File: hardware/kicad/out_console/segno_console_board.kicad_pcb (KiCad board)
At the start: 2 copper layers, 130 x 90 mm, 53 parts, among them J1 RaspberryPi_Pico_Common_THT, J10 JST_XH_B2B-XH-A_1x02_P2.50mm_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, J11 JST_XH_B2B-XH-A_1x02_P2.50mm_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, J12 JST_XH_B2B-XH-A_1x02_P2.50mm_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, J13 JST_XH_B2B-XH-A_1x02_P2.50mm_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, J14 JST_XH_B2B-XH-A_1x02_P2.50mm_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, J15 JST_XH_B2B-XH-A_1x02_P2.50mm_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, J16 JST_XH_B2B-XH-A_1x02_P2.50mm_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, J17 JST_XH_B2B-XH-A_1x02_P2.50mm_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, J18 JST_XH_B2B-XH-A_1x02_P2.50mm_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, J19 JST_XH_B2B-XH-A_1x02_P2.50mm_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, J2 IDC-Header_2x20_P2.54mm_Verti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, J20 JST_XH_B3B-XH-A_1x03_P2.50mm_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, J21 JST_XH_B3B-XH-A_1x03_P2.50mm_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, J3 JST_XH_B4B-XH-A_1x04_P2.50mm_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, J4 JST_XH_B3B-XH-A_1x03_P2.50mm_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, J5 JST_XH_B2B-XH-A_1x02_P2.50mm_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, J6 JST_XH_B8B-XH-A_1x08_P2.50mm_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, J7 JST_XH_B3B-XH-A_1x03_P2.50mm_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, J8 JST_XH_B2B-XH-A_1x02_P2.50mm_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, J9 JST_XH_B3B-XH-A_1x03_P2.50mm_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, U1 DIP-14_W7.62mm, U2 DIP-6_W7.62mm

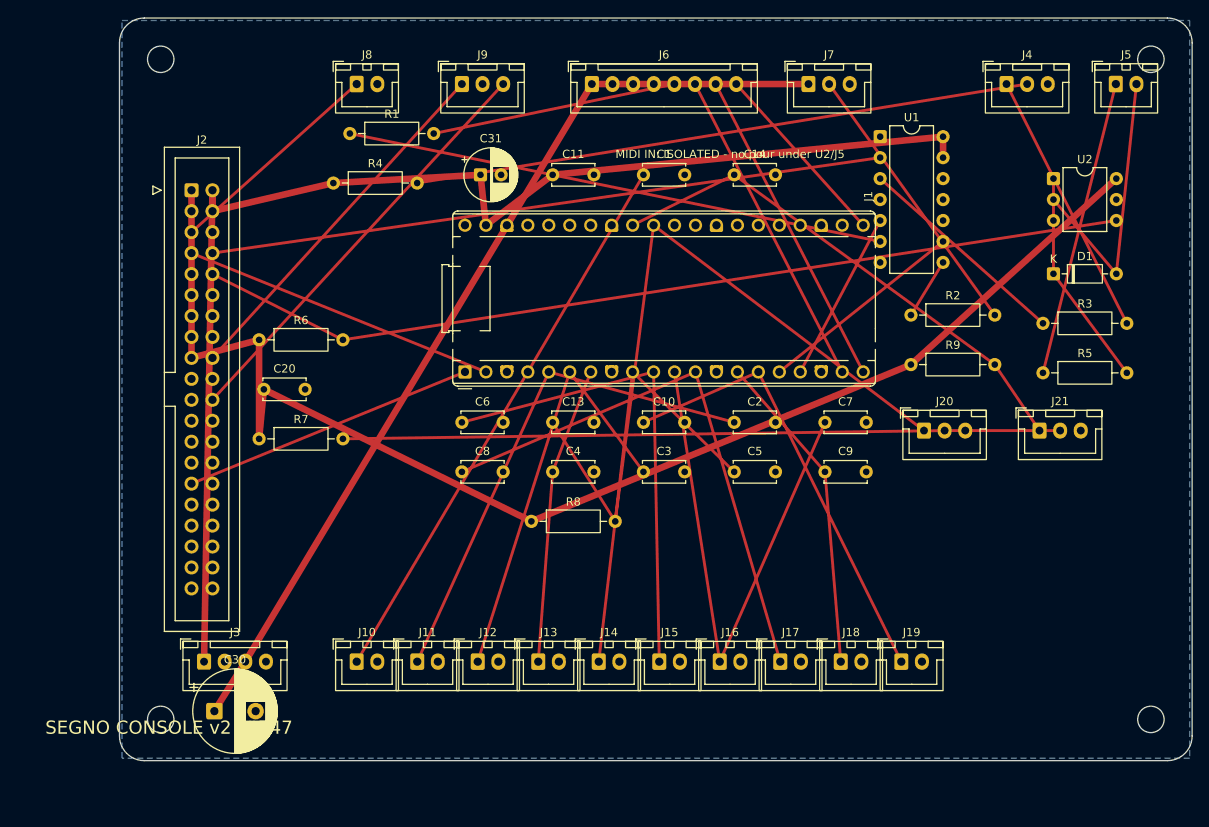
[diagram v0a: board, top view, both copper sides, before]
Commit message: feat(hardware): lay out the console board around its harness, not its schematic
The v2 board placed connectors wherever they fit. Reworked so the two things
that actually constrain it drive the layout:

- The pin map is half the floorplan. The module's pads 1..20 are one physical
  row and 21..40 the other, so a GPIO number decides where a connector can sit.
  LINK moves to GP16/17 (still a UART0 pair, now the end nearest the ribbon),
  the ring/encoder group onto four contiguous row-A pads, and gates enforce
  both. ENC_B used to run 42 mm diagonally across the board.
- Connectors group by where their CABLE goes. POWER, MIDI IN, MIDI OUT, CTRL 1
  and CTRL 2 all land on the rear panel, so they sit on one edge in the panel's
  own order, gated against rear_io_stations.json. The loom used to leave the
  board from two places.

Also: the Pi ribbon moves to the board edge (a 40-way leaving mid-board folds
back over everything), ground pours on both layers, every connector carries a
function label like segno_pedal_main does, and an expansion header exposes the
six GPIO that were being ERC-exempted into nothing.

115x95 mm, down from 160x100. 0 DRC violations, 0 unconnected.

New gates, each negative-controlled: RATSNEST (total MST copper), HOP (no part
stranded from what it wires to), REAR_ORDER, PAD_ROW, LINK_UART, SILK (off-board
or over-a-part text). Fixed ISOLATION, which exempted every ref starting R/C/D
and so could not fail for the likeliest mistake there is.

Refs #747
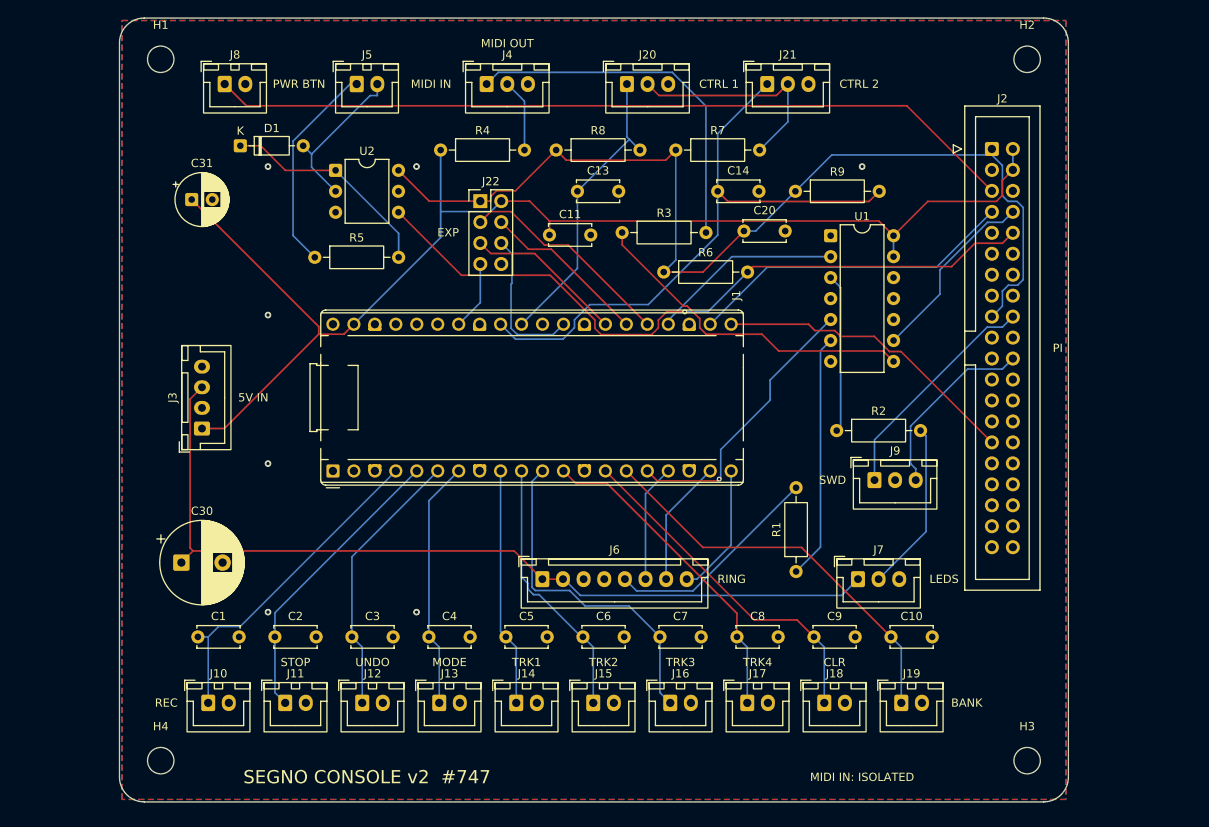
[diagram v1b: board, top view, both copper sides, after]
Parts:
- removed ? (x4): , 
- added H1: MountingHole_3.2mm_M3, MountingHole_3.2mm_M3, F.Cu at (105.0, 65.0)
- added H2: MountingHole_3.2mm_M3, MountingHole_3.2mm_M3, F.Cu at (210.0, 65.0)
- added H3: MountingHole_3.2mm_M3, MountingHole_3.2mm_M3, F.Cu at (210.0, 150.0)
- added H4: MountingHole_3.2mm_M3, MountingHole_3.2mm_M3, F.Cu at (105.0, 150.0)
- added J22: PinHeader_2x04_P2.54mm_Vertical, PinHeader_2x04_P2.54mm_Vertical, F.Cu at (143.7, 82.2)
- moved D1 99.8 mm to (114.6, 75.5)
- moved J2 97.1 mm to (205.7, 75.9)
- moved J5 92.0 mm to (128.8, 68.0)
- moved R5 89.4 mm to (123.7, 89.0)
- moved U2 87.0 mm to (126.2, 78.5)
- moved C1 77.8 mm to (109.5, 135.0)
- moved R1 75.8 mm to (182.0, 127.1), turned to 90 degrees
- moved J9 69.3 mm to (191.5, 116.0)
- moved J4 63.0 mm to (144.5, 68.0)
- moved R7 61.4 mm to (167.4, 76.0)
- moved C2 61.4 mm to (118.8, 135.0)
- moved C20 61.3 mm to (175.7, 85.8)
- moved J6 60.3 mm to (151.2, 128.0)
- moved J7 60.3 mm to (189.5, 128.0)
- moved J20 55.3 mm to (161.5, 68.0)
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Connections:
- J1 pad 1: LINK_TX -> (no net)
- J1 pad 16: IND_DATA -> RING_DATA
- J1 pad 17: RING_DATA -> ENC_A
- J1 pad 19: ENC_A -> ENC_B
- J1 pad 2: LINK_RX -> (no net)
- J1 pad 20: ENC_B -> ENC_SW
- J1 pad 21: ENC_SW -> LINK_TX
- J1 pad 22: (no net) -> LINK_RX
- J1 pad 24: (no net) -> IND_DATA
- J1 pad 25: (no net) -> EXP_GP19
- J1 pad 26: (no net) -> EXP_GP20
- J1 pad 27: (no net) -> EXP_GP21
- J1 pad 29: (no net) -> EXP_GP22
- J1 pad 34: (no net) -> EXP_GP28
- U1 pad 2: MIDI_TX -> IND_DATA
- U1 pad 3: MIDI_OUT_BUF -> IND_DATA_BUF
- U1 pad 8: IND_DATA_BUF -> MIDI_OUT_BUF
- U1 pad 9: IND_DATA -> MIDI_TX
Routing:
- net PWR_BTN: track 26.9 -> 98.3 mm
- net N$2: track 74.9 -> 8.86 mm
- net CTRL_REF: track 86.9 -> 27.6 mm
- net MIDI_TX: track 81.7 -> 22.6 mm
- net CTRL1_TIP: track 91.5 -> 36.5 mm
- net +3V3: track 166.3 -> 124.9 mm
- net RING_DATA_BUF: track 65.6 -> 29.7 mm
- net SWDIO: track 52.0 -> 22.6 mm
- net SW_RECPLAY: track 68.5 -> 40.3 mm
- net SW_TRACK4: track 67.4 -> 39.5 mm
- net SW_TRACK2: track 59.1 -> 32.2 mm
- net EXP_GP19: track 0.00 -> 26.4 mm
- net SW_STOP: track 61.8 -> 35.8 mm
- net SW_TRACK3: track 67.2 -> 41.1 mm
- net MIDI_RX: track 112.5 -> 86.8 mm, vias 0 -> 1
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- added copper zone on F.Cu, net GND
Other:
- board size 130 x 90 mm -> 115 x 95 mm
- board text added: "5V IN"
- board text added: "BANK"
- board text added: "CLR"
- board text added: "CTRL 1"
- board text added: "CTRL 2"
- board text added: "EXP"
- board text added: "LEDS"
- board text added: "MIDI IN"
- board text added: "MIDI IN: ISOLATED"
- board text added: "MIDI OUT"
- board text added: "MODE"
- board text added: "PI"
- board text added: "PWR BTN"
- board text added: "REC"
- board text added: "RING"
- board text added: "STOP"
- board text added: "SWD"
- board text added: "TRK1"
- board text added: "TRK2"
- board text added: "TRK3"
- board text added: "TRK4"
- board text added: "UNDO"
- board text removed: "MIDI IN: ISOLATED - no pour under U2/J5"

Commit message: style(hardware): put the console board's connectors and labels on shared lines
Purely cosmetic; no net or gate changes. The board read as scattered because
three separate things were each individually legal and collectively arbitrary:

- The rear-panel headers sat at 14/30/47/64/81 -- three different gaps, and the
  group off-centre. They are now on an even 17.5 mm pitch centred on x 54, the
  same centre line the switch row already used, and the resistors below them sit
  on those same centres rather than a 15 mm pitch of their own. Two pitches
  beating against each other is what made the band look crooked.
- Labels were placed by a nearest-free-gap search, so the rear-panel row came out
  "above, right, above, right, right" and REC sat left of its header while its
  nine neighbours sat above. The two rows that matter are now pinned to one y;
  the search remains as fallback for one-off headers.
- R1 was the only vertical resistor among twelve horizontals, which reads as an
  accident rather than a decision.

Still 0 DRC violations, 0 unconnected.

Refs #747
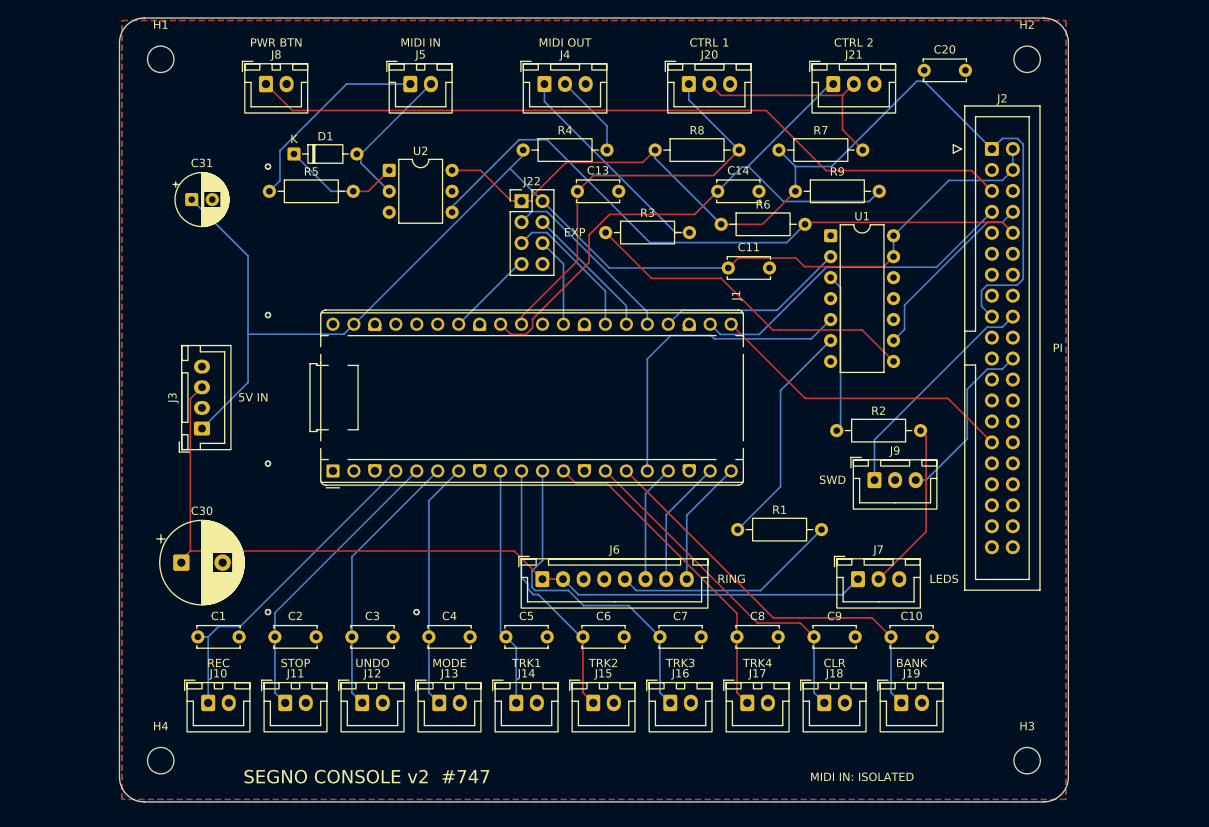
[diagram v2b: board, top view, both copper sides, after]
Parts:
- moved C20 29.3 mm to (197.5, 66.3)
- moved C11 22.0 mm to (173.8, 90.3)
- moved R7 12.5 mm to (179.9, 76.0)
- moved R8 12.0 mm to (164.9, 76.0)
- moved R4 10.0 mm to (148.9, 76.0)
- moved R5 9.71 mm to (118.2, 81.0)
- moved R6 9.05 mm to (172.9, 85.0)
- moved R1 8.71 mm to (174.9, 122.0), turned to 0 degrees
- moved J21 8.00 mm to (186.5, 68.0)
- moved J20 7.50 mm to (169.0, 68.0)
- moved J4 7.00 mm to (151.5, 68.0)
- moved D1 6.58 mm to (121.1, 76.5)
- moved J5 6.50 mm to (135.2, 68.0)
- moved U2 6.50 mm to (132.7, 78.5)
- moved J22 5.00 mm to (148.7, 82.2)
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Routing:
- net N$1: track 44.2 -> 26.3 mm
- net CTRL1_TIP: track 36.5 -> 51.1 mm
- net N$4: track 26.5 -> 14.5 mm
- net MIDI_RX: track 86.8 -> 78.7 mm, vias 1 -> 0
- net EXP_GP22: track 18.1 -> 10.9 mm
- net PWR_BTN: track 98.3 -> 93.3 mm
- net EXP_GP19: track 26.4 -> 22.3 mm
- net +3V3: track 124.9 -> 120.9 mm
- net RING_DATA: track 34.2 -> 38.1 mm, vias 1 -> 0
- net EXP_GP20: track 20.3 -> 16.6 mm
- net +5V: track 154.6 -> 151.6 mm
- net EXP_GP28: track 8.39 -> 10.6 mm
- net RING_DATA_BUF: track 29.7 -> 27.6 mm
- net EXP_GP21: track 19.2 -> 17.6 mm
- net CTRL_REF: track 27.6 -> 26.3 mm
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
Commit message: style(hardware): align J7 with J9 on the console board
Same 3-pin footprint, one directly below the other, sitting 2 mm apart in x --
which reads as a slip rather than a decision. No net changes; still 0 DRC
violations, 0 unconnected.

Refs #747
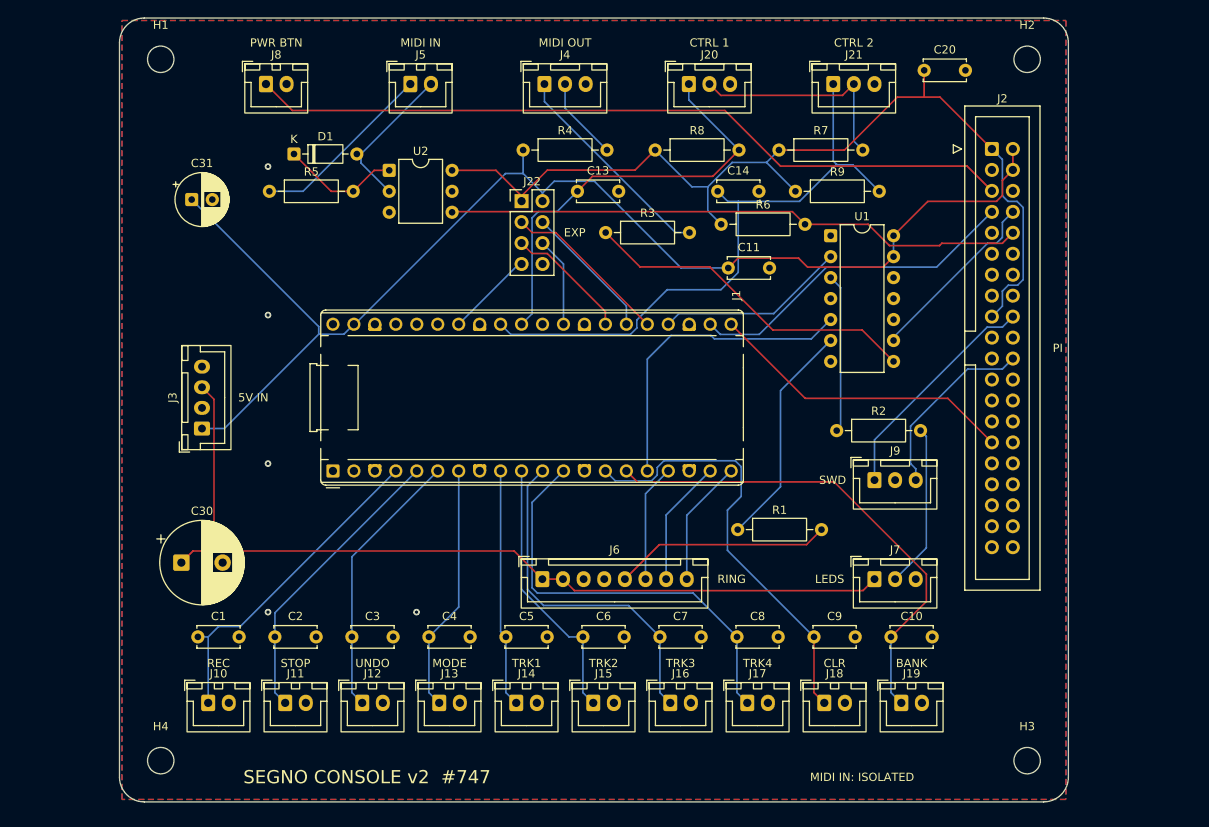
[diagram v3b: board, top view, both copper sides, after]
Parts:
- moved J7 2.00 mm to (191.5, 128.0)
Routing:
- net SW_TRACK4: track 39.5 -> 51.6 mm
- net SW_CLEAR: track 42.1 -> 53.0 mm
- net SW_BANK: track 48.9 -> 59.4 mm
- net MIDI_RX: track 78.7 -> 70.3 mm
- net +3V3: track 120.9 -> 116.8 mm
- net +5V: track 151.6 -> 154.4 mm
- net EXP_GP21: track 17.6 -> 15.1 mm
- net N$3: track 24.6 -> 22.5 mm
- net EXP_GP19: track 22.3 -> 20.4 mm
- net +5V_LED: track 106.2 -> 107.6 mm
- net CTRL1_TIP: track 51.1 -> 52.4 mm
- net SWDIO: track 21.4 -> 22.6 mm
- net RING_DATA_OUT: track 27.5 -> 26.3 mm
- net SW_TRACK3: track 41.1 -> 42.1 mm
- net CTRL_REF: track 26.3 -> 27.1 mm
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
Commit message: feat(hardware): solder SWD to the Pico's own debug pads and centre the rows
The board would not route: RING_DATA had to climb from the module's row A to
U1's input through the corridor that the link, IND, EXP and CTRL nets all cross,
and J9 -- a 3-pin header breaking SWD out to flying wires -- sat in it. Centring
the pedal row made that corridor tighter still, so the two problems were one.

Both go away by dropping J9. Module:RaspberryPi_Pico_SMD_HandSolder carries the
three debug pads (D1/D2/D3) that the THT footprint does not, so SWCLK/GND/SWDIO
land straight on the module. The connector, its wires and the space it occupied
are gone. Conn_01x40 has no D pins, so they are added to the part explicitly --
otherwise SWD silently has nothing to attach to.

Trade: the module is soldered by its castellations, not socketed on headers, so
swapping one needs hot air. For a sealed console reflashed over SWD, correct.

Also: both connector rows now sit on the board's true centre (x 57.5) at an even
17.5 mm pitch -- the pedal row was 7.75 mm from the left edge and 14.75 from the
right -- and freerouting runs with -dct 0, cutting its 20 s idle timeout.

115x96 mm. 0 DRC violations, 0 unconnected, and it routes clean first attempt
rather than one roll in three.

Refs #747
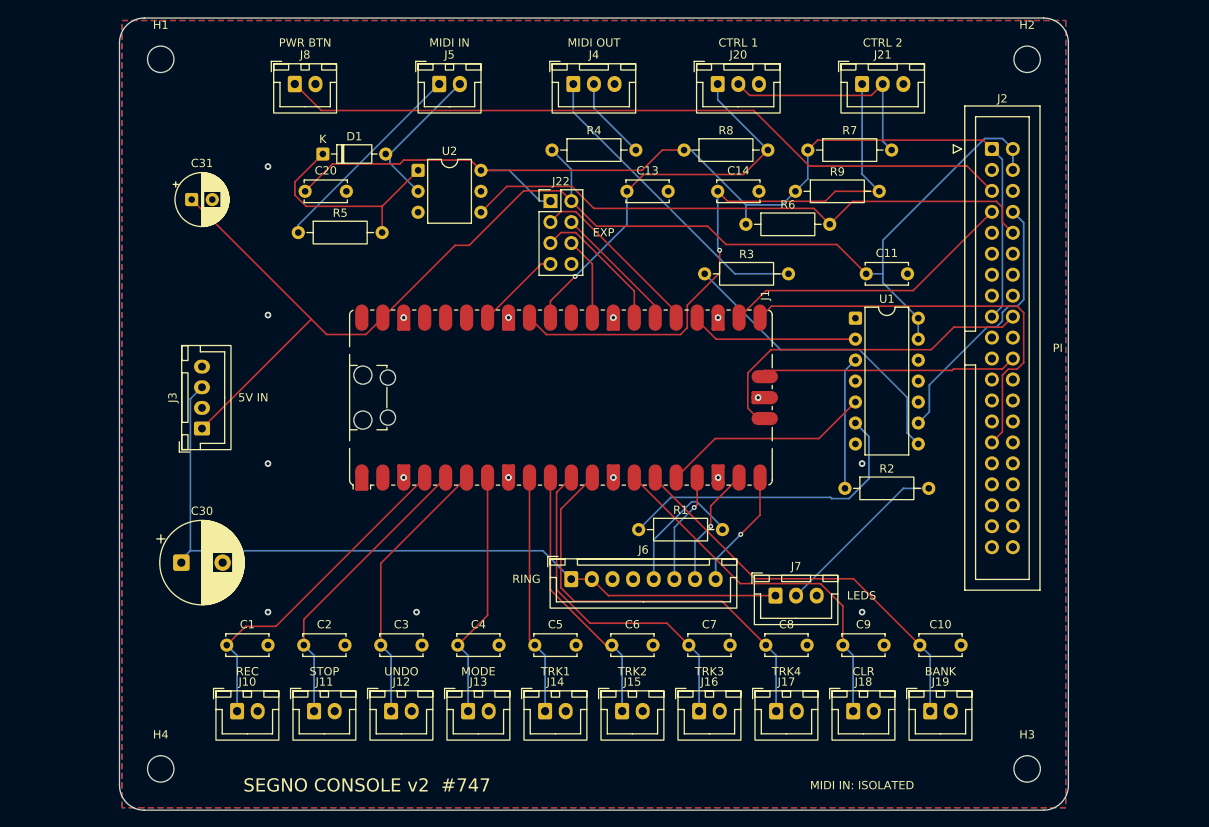
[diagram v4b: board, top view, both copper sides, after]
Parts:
- removed J9: JST_XH_B3B-XH-A_1x03_P2.50mm_Vertical, JST_XH_B3B-XH-A_1x03_P2.50mm_Vertical
- J1: value RaspberryPi_Pico_Common_THT -> RaspberryPi_Pico_SMD_HandSolder; footprint RaspberryPi_Pico_Common_THT -> RaspberryPi_Pico_SMD_HandSolder
- moved C20 76.4 mm to (122.5, 81.0)
- moved J1 29.0 mm to (153.5, 106.0)
- moved C11 16.7 mm to (190.5, 91.0)
- moved R3 13.0 mm to (170.9, 91.0)
- moved J7 12.2 mm to (179.5, 130.0)
- moved R1 12.0 mm to (162.9, 122.0)
- moved U1 10.4 mm to (189.2, 96.4)
- moved R2 7.07 mm to (187.9, 117.0)
- moved R5 6.10 mm to (121.7, 86.0)
- moved C13 6.00 mm to (161.5, 81.0)
- moved C1 3.64 mm to (113.0, 136.0)
- moved C10 3.64 mm to (197.0, 136.0)
- moved C2 3.64 mm to (122.3, 136.0)
- moved C3 3.64 mm to (131.7, 136.0)
- moved C4 3.64 mm to (141.0, 136.0)
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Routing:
- net LINK_TX: track 37.5 -> 50.8 mm
- net SWCLK: track 27.8 -> 41.0 mm
- net RING_DATA: track 38.1 -> 25.5 mm
- net N$4: track 14.5 -> 26.9 mm
- net +5V_LED: track 107.6 -> 95.4 mm
- net +3V3: track 116.8 -> 128.5 mm
- net N$1: track 26.3 -> 37.6 mm
- net +5V: track 154.4 -> 165.5 mm
- net MIDI_TX: track 22.2 -> 32.7 mm
- net RING_DATA_BUF: track 27.6 -> 38.0 mm
- net SW_BANK: track 59.4 -> 49.1 mm
- net RING_DATA_OUT: track 26.3 -> 16.6 mm
- net SWDIO: track 22.6 -> 31.8 mm
- net SW_CLEAR: track 53.0 -> 45.0 mm
- net LINK_RX: track 40.8 -> 36.0 mm
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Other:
- board size 115 x 95 mm -> 115 x 96 mm
- board text removed: "SWD"
